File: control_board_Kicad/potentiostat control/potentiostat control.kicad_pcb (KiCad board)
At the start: 2 copper layers, 83 x 46 mm, 8 parts, among them J1 L717SDA15PA4CH4F, Q1 2N7002, Q2 2N7002, SW1 3-1825910-5, U1 Raspberry Pi Pico

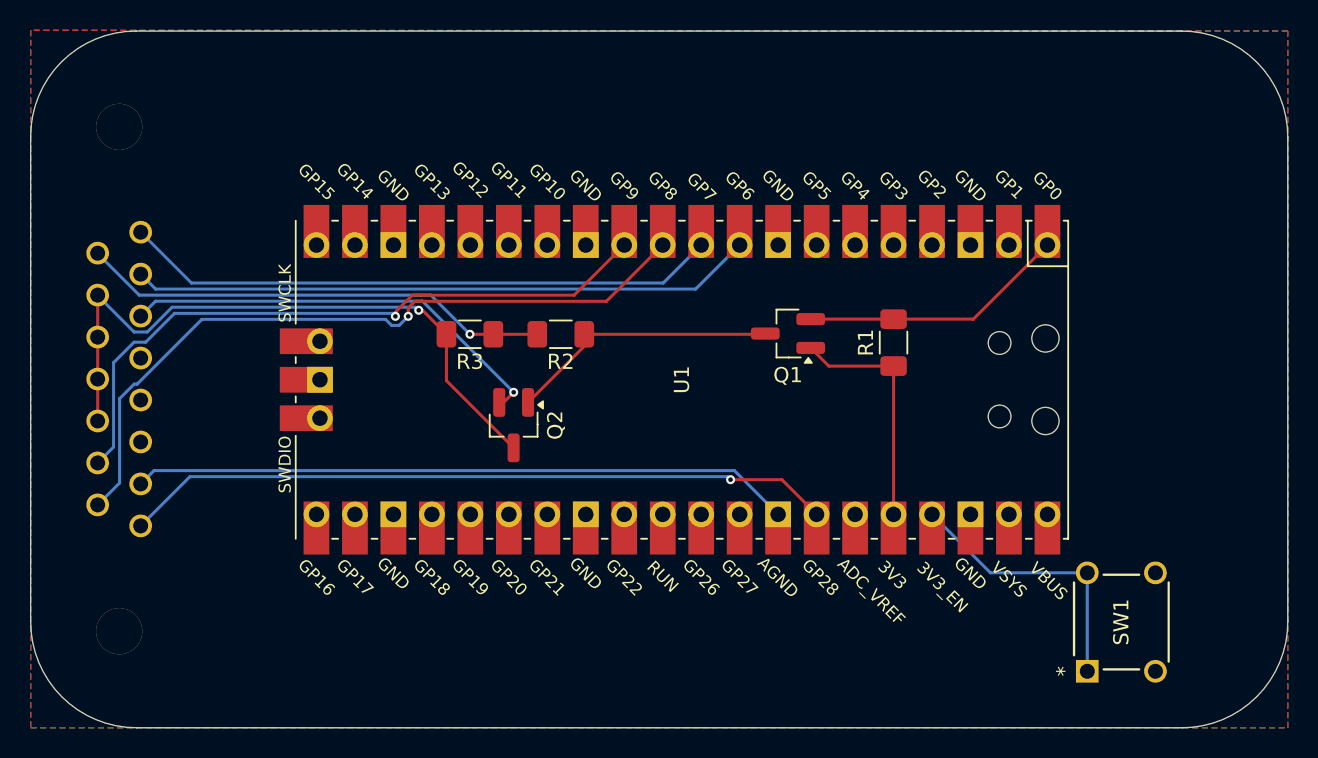
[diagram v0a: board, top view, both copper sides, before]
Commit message: add autosampler design
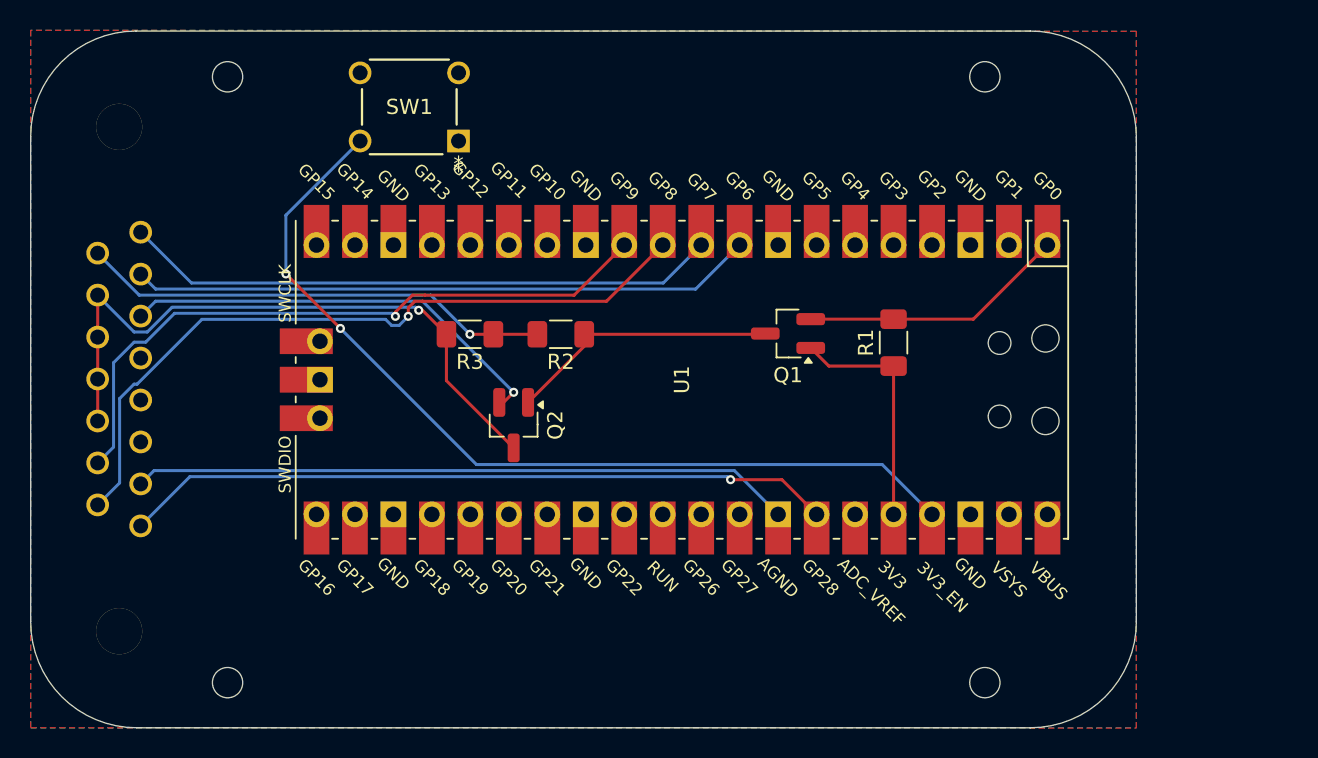
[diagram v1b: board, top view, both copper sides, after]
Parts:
- added REF**: MountingHole_2mm, MountingHole:MountingHole_2mm, F.Cu at (150.0, 120.0)
- added REF**: MountingHole_2mm, MountingHole:MountingHole_2mm, F.Cu at (100.0, 120.0)
- added REF**: MountingHole_2mm, MountingHole:MountingHole_2mm, F.Cu at (150.0, 80.0)
- added REF**: MountingHole_2mm, MountingHole:MountingHole_2mm, F.Cu at (100.0, 80.0)
- moved SW1 62.0 mm to (108.8, 79.7), turned to 180 degrees
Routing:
- net Net-(U1-3V3_EN): track 18.3 -> 60.0 mm, vias 0 -> 2
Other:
- board size 83 x 46 mm -> 73 x 46 mm

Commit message: update board
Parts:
- J1: value L717SDA15PA4CH4F -> L717HDE15PD1CH4F; footprint DB15:CONN_L717SDA15PA4CH4F_AMP -> DB15_L717HDE15PD1CH4F:AMPHENOL_L717HDE15PD1CH4F
- moved J1 13.1 mm to (96.5, 100.2), turned to 90 degrees
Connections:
- J1 pad 6: DGND -> GND
- Q2 pad 2: DGND -> GND
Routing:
- net DGND: track 28.5 -> 0.00 mm, vias 1 -> 0
- net Net-(U1-GP7): track 39.4 -> 66.6 mm, vias 0 -> 1
- net Net-(U1-GP6): track 41.2 -> 61.7 mm, vias 0 -> 1
- net Net-(U1-GP9): track 44.3 -> 32.5 mm
- net Net-(U1-GP8): track 48.3 -> 37.0 mm
- net Net-(Q2-D): track 43.1 -> 53.5 mm, vias 1 -> 2
- net Net-(Q1-D): track 17.9 -> 24.0 mm, vias 0 -> 2
- net Net-(U1-3V3_EN): track 60.0 -> 66.0 mm
- net Net-(U1-GP28): track 47.0 -> 41.7 mm
- net AGND: track 43.3 -> 40.1 mm
- net +5VP: track 31.2 -> 29.1 mm
- net GND: track 0.00 -> 1.13 mm, vias 0 -> 1
